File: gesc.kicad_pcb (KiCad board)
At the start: 4 copper layers, 111 x 111 mm, 154 parts, among them J1 Conn_01x06, J10 PHASE_C, J11 PHASE_B, J12 NTC, J13 T-Motor, J14 Conn_01x03, J15 EXT_OFF, J2 Conn_01x06, J3 Conn_01x06, J4 Conn_01x05, J5 Conn_01x03, J6 USB_B_Mini, J7 BAT+, J8 BAT-, J9 PHASE_A, Q1 BSC070N10NS5, Q2 BSC070N10NS5, Q3 BSC070N10NS5, Q4 BSC070N10NS5, Q5 BSC070N10NS5, Q6 BSC070N10NS5, U1 STM32F405RGTx, U10 LM5008MM, U11 SN74LVC1G66DBVR, U12 LM5107, U13 SN74LVC1G66DBVR, U14 AQY282S, U15 LM5107, U16 EYSGJNZWY, U17 LMR12010YMKE_NOPB, U2 SN74LVC1G66DBVR, U3 LM5107, U4 INA240A1, U5 INA240A1, U6 INA240A1, U7 SN74LVC1G66DBVR, U8 SN74LVC1G66DBVR, U9 SN74LVC1G66DBVR, Y1 X50328MSB2GI

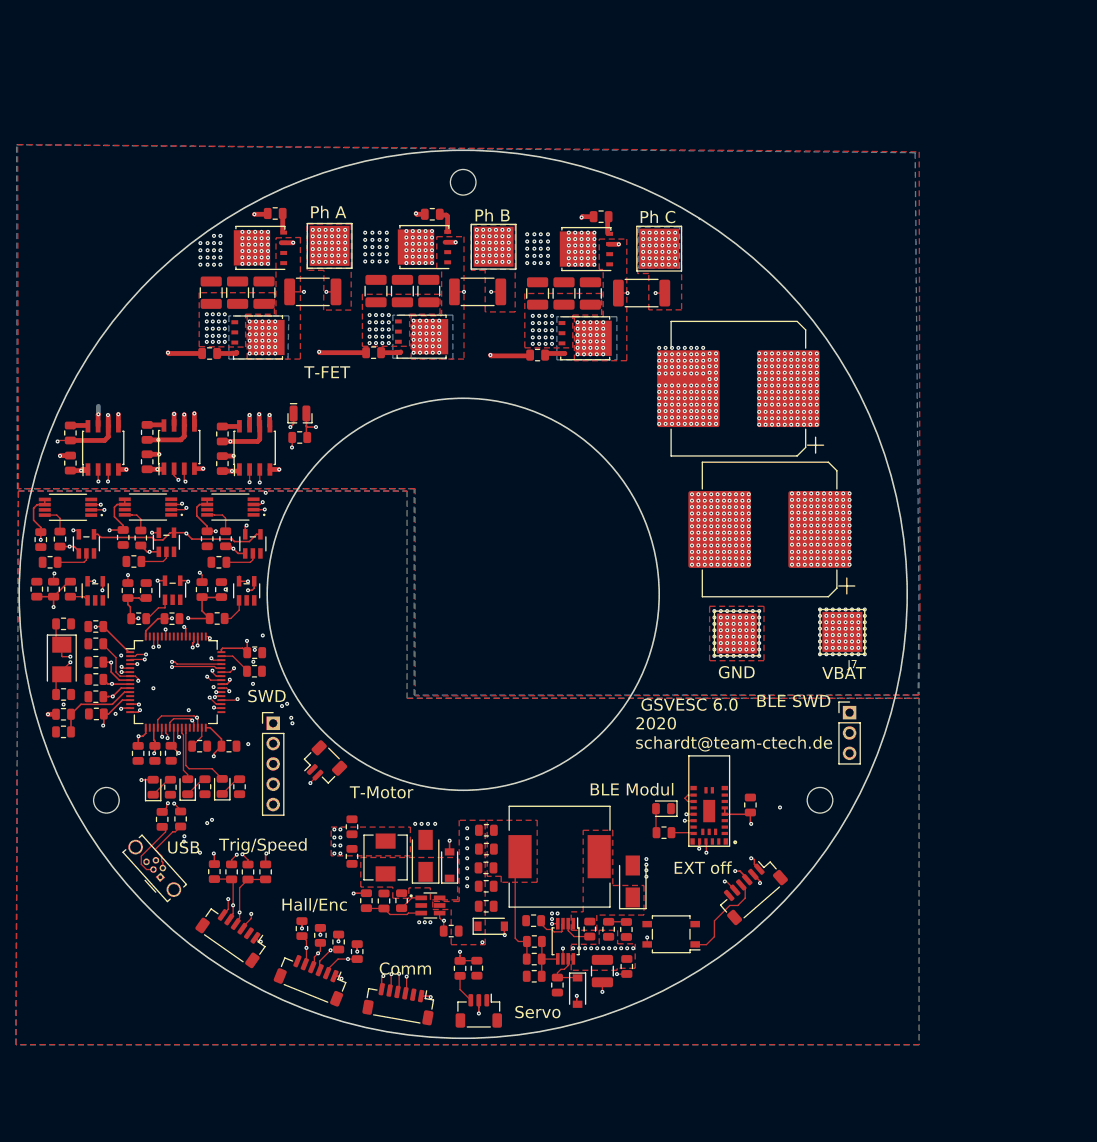
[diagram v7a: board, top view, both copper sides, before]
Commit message: |--- Add Schottky between phase and gnd at HS pin of LM5107 |--- Add 5R6 in phase line to HS pin of LM5107 |--- Change high side bypass cap to 10u/25V |--- Add 14V TVS diode parallel to high side bypass cap |--- Add one 12V TVS diode to 12V near driver |--- move gate tracks and back from side by side to on top of each other
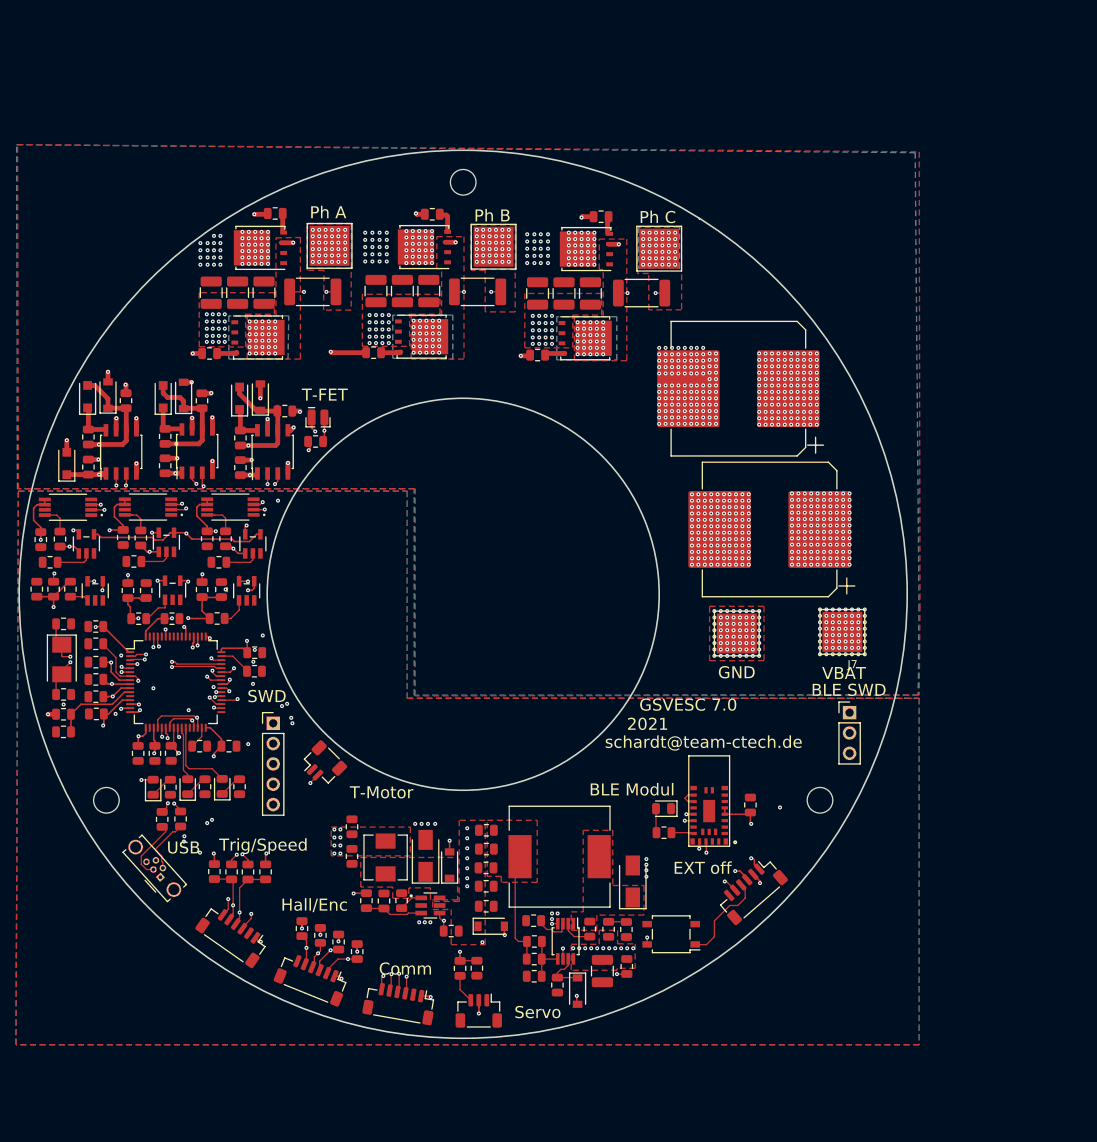
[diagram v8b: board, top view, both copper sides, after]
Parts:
- added D10: MBR2H100SFTN, Diode_SMD:D_SOD-123, F.Cu at (65.0, 75.1)
- added D12: MBR2H100SFTN, Diode_SMD:D_SOD-123, F.Cu at (74.6, 75.3)
- added D13: SMF14A, Diode_SMD:D_SOD-123F, F.Cu at (53.0, 75.3)
- added D14: SMF14A, Diode_SMD:D_SOD-123F, F.Cu at (62.5, 75.3)
- added D15: SMF14A, Diode_SMD:D_SOD-123F, F.Cu at (72.0, 75.5)
- added D16: SMF12A, Diode_SMD:D_SOD-123F, F.Cu at (50.4, 83.6)
- added D9: MBR2H100SFTN, Diode_SMD:D_SOD-123, F.Cu at (55.6, 75.1)
- added R47: 5r60, Resistor_SMD:R_0805_2012Metric, F.Cu at (57.8, 75.8)
- added R48: 5r60, Resistor_SMD:R_0805_2012Metric, F.Cu at (67.3, 75.8)
- added R49: 5r60, Resistor_SMD:R_0805_2012Metric, F.Cu at (77.7, 77.1)
- C21, C27, C32: value 100n -> 10u0/25V
- R25, R26, R28, R32, R42, R43: value 10r0 -> 5r60
- moved C15 2.30 mm to (53.1, 84.1)
- moved C21 2.30 mm to (53.1, 80.3)
- moved C22 2.30 mm to (62.7, 83.9)
- moved C27 2.30 mm to (62.7, 80.3)
- moved C29 2.30 mm to (72.1, 84.2)
- moved C32 2.30 mm to (72.1, 80.5)
- moved J12 2.30 mm to (81.8, 76.7)
- moved U12 2.30 mm to (66.7, 82.1)
- moved U15 2.30 mm to (76.2, 82.2)
- moved U3 2.30 mm to (57.2, 82.2)
- moved R36 2.05 mm to (81.5, 80.9)
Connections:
- C21 pad 2: /Driver/SH_A -> /Driver/SH_A_R
- C27 pad 2: /Driver/SH_B -> /Driver/SH_B_R
- C32 pad 2: /Driver/SH_C -> /Driver/SH_C_R
- R13 pad 1: /Driver/SH_A -> /Driver/SH_A_R
- R17 pad 1: /Driver/SH_B -> /Driver/SH_B_R
- R19 pad 1: /Driver/SH_C -> /Driver/SH_C_R
- U12 pad 6: /Driver/SH_B -> /Driver/SH_B_R
- U15 pad 6: /Driver/SH_C -> /Driver/SH_C_R
- U3 pad 6: /Driver/SH_A -> /Driver/SH_A_R
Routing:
- net /Driver/SH_A_R: track 0.00 -> 36.1 mm, vias 0 -> 2
- net /Driver/SH_B_R: track 0.00 -> 35.9 mm, vias 0 -> 2
- net /Driver/SH_C_R: track 0.00 -> 35.3 mm, vias 0 -> 2
- net /Driver/SH_B: track 138.1 -> 104.3 mm, vias 36 -> 34
- net /Driver/SH_C: track 154.4 -> 122.9 mm, vias 36 -> 34
- net /Driver/SH_A: track 117.7 -> 86.7 mm, vias 36 -> 34
- net GND: track 120.5 -> 116.6 mm, vias 387 -> 390
- net Net-(C21-Pad1): track 2.34 -> 5.08 mm
- net Net-(C27-Pad1): track 2.13 -> 4.85 mm
- net /Driver/GH_B: track 47.8 -> 45.1 mm
- net Net-(C32-Pad1): track 2.14 -> 4.81 mm
- net /Driver/GL_B: track 27.5 -> 24.8 mm
- net /Driver/GL_C: track 37.1 -> 34.9 mm
- net /Driver/GH_A: track 38.5 -> 36.6 mm
- net /Driver/GH_C: track 57.9 -> 56.1 mm
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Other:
- board text added: "2021"
- board text added: "GSVESC 7.0"
- board text added: "schardt@team-ctech.de"
- board text removed: "2020 schardt@team-ctech.de"
- board text removed: "GSVESC 6.0"
